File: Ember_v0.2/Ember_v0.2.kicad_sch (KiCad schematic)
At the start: 57 parts, among them J3 DROGUE, J4 BATT_CONN, J5 MAIN, J6 MAN2, J7 DROGUE2, J8 ARM, Q1 SISA96DN-T1, Q2 SISA96DN-T1, Q3 SISA96DN-T1, Q4 SISA96DN-T1, Q5 CJ3400, U1 LDO Regulator 5v, U2 BNO055, U4 BMP280, U5 BMI160, U7 RPi Pico 2

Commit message: Roughly added the strain gauge thingy
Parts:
- added C3, C4, C8, C9: 100nF, microbuilder:0603, symbol microbuilder:CAP_CERAMIC0603
- added R10, R11, R12, R16, R18, R25, R26, R34, R35, R36, R37, R9: 330E, microbuilder:0603, symbol microbuilder:RESISTOR0603
- added U6, U8: ADS1220xPW, Package_SO:TSSOP-16_4.4x5mm_P0.65mm, symbol Analog_ADC:ADS1220xPW
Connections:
- net 3v3: now also C3.1 (P$1), C4.1 (P$1), C8.1 (P$1), C9.1 (P$1), R11.2, R18.2, R34.2, R37.2, U6.12 (AVDD), U6.13 (DVDD), U6.9 (REFP0), U8.12 (AVDD), U8.13 (DVDD), U8.9 (REFP0)
- net GND: now also C3.2 (P$2), C4.2 (P$2), C8.2 (P$2), C9.2 (P$2), R10.1, R12.1, R16.1, R25.1, R26.1, R35.1, R36.1, R9.1, U6.3 (CLK), U6.4 (DGND), U6.5 (AVSS), U6.8 (REFN0), U8.3 (CLK), U8.4 (DGND), U8.5 (AVSS), U8.8 (REFN0)
- net GPS_RX: no longer U7.P$6 (GP4)
- net GPS_TX: no longer U7.P$7 (GP5)
- net LORA_BUSY: no longer names the net of U7.P$12 (GP9)
- net LORA_CS: no longer names the net of U7.P$17 (GP13)
- net LORA_DIO1: no longer names the net of U7.P$15 (GP11)
- net LORA_MISO: no longer names the net of U7.P$11 (GP8)
- net LORA_MOSI: no longer names the net of U7.P$20 (GP15)
- net LORA_RESET: no longer names the net of U7.P$16 (GP12)
- net LORA_SCLK: no longer names the net of U7.P$19 (GP14)
- new net ACT1: R10.2, U6.11 (AIN0/REFP1)
- new net ACT2: R16.2, U6.7 (AIN2)
- new net ACT3: R26.2, U8.11 (AIN0/REFP1)
- new net ACT4: R36.2, U8.7 (AIN2)
- new net ADS_CS_1: U6.2 (~{CS})
- new net ADS_CS_2: U8.2 (~{CS})
- new net ADS_DRDY_1: U6.14 (~{DRDY})
- new net ADS_DRDY_2: U8.14 (~{DRDY})
- new net ADS_MISO: U6.15 (DOUT/~{DRDY}), U8.15 (DOUT/~{DRDY})
- new net ADS_MOSI: U6.16 (DIN), U8.16 (DIN)
- new net ADS_SCLK: U6.1 (SCLK), U8.1 (SCLK)
- new net REF1: R11.1, R9.2, U6.10 (AIN1)
- new net REF2: R12.2, R18.1, U6.6 (AIN3/REFN1)
- new net REF3: R25.2, R34.1, U8.10 (AIN1)
- new net REF4: R35.2, R37.1, U8.6 (AIN3/REFN1)
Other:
- moved on the sheet: C1, C13, C14, C15, C16, C2, C24, C25, LS2, Q1, Q2, Q3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

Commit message: anything until test launch prep
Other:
- moved on the sheet: C14, R19, R24, U4
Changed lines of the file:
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@@
 	(text "BMP280"
 		(exclude_from_sim no)
-		(at 360.934 167.386 0)
+		(at 354.584 190.246 0)
 		(effects
 			(font
@@
 	)
 	(junction
-		(at 367.03 154.94)
+		(at 360.68 177.8)
 		(diameter 0)
 		(color 0 0 0 0)
@@
 	)
 	(junction
-		(at 364.49 133.35)
+		(at 358.14 156.21)
 		(diameter 0)
 		(color 0 0 0 0)
@@
 	(wire
 		(pts
-			(xy 346.71 147.32) (xy 354.33 147.32)
+			(xy 340.36 170.18) (xy 347.98 170.18)
 		)
 		(stroke
@@
 	(wire
 		(pts
-			(xy 364.49 154.94) (xy 367.03 154.94)
+			(xy 358.14 177.8) (xy 360.68 177.8)
 		)
 		(stroke
@@
 	(wire
 		(pts
-			(xy 332.74 147.32) (xy 336.55 147.32)
+			(xy 326.39 170.18) (xy 330.2 170.18)
 		)
 		(stroke
@@
 	(wire
 		(pts
-			(xy 346.71 142.24) (xy 354.33 142.24)
+			(xy 340.36 165.1) (xy 347.98 165.1)
 		)
 		(stroke
@@
 	(wire
 		(pts
-			(xy 364.49 130.81) (xy 364.49 133.35)
+			(xy 358.14 153.67) (xy 358.14 156.21)
 		)
 		(stroke
@@
 	(wire
 		(pts
-			(xy 364.49 137.16) (xy 364.49 133.35)
+			(xy 358.14 160.02) (xy 358.14 156.21)
 		)
 		(stroke
@@
 	(wire
 		(pts
-			(xy 354.33 149.86) (xy 354.33 153.67)
+			(xy 347.98 172.72) (xy 347.98 176.53)
 		)
 		(stroke
@@
 	(wire
 		(pts
-			(xy 346.71 144.78) (xy 354.33 144.78)
+			(xy 340.36 167.64) (xy 347.98 167.64)
 		)
 		(stroke
@@
 	(wire
 		(pts
-			(xy 367.03 154.94) (xy 367.03 160.02)
+			(xy 360.68 177.8) (xy 360.68 182.88)
 		)
 		(stroke
@@
 	(wire
 		(pts
-			(xy 367.03 133.35) (xy 364.49 133.35)
+			(xy 360.68 156.21) (xy 358.14 156.21)
 		)
 		(stroke
@@
 	(wire
 		(pts
-			(xy 354.33 133.35) (xy 356.87 133.35)
+			(xy 347.98 156.21) (xy 350.52 156.21)
 		)
 		(stroke
@@
 	(wire
 		(pts
-			(xy 367.03 133.35) (xy 367.03 137.16)
+			(xy 360.68 156.21) (xy 360.68 160.02)
 		)
 		(stroke
@@
 	)
 	(label "3v3"
-		(at 344.17 153.67 0)
+		(at 337.82 176.53 0)
 		(effects
 			(font
@@
 	)
 	(label "GND"
-		(at 354.33 133.35 180)
+		(at 347.98 156.21 180)
 		(effects
 			(font
@@
 	)
 	(label "GND"
-		(at 332.74 147.32 180)
+		(at 326.39 170.18 180)
 		(effects
 			(font
@@
 	)
 	(label "GND"
-		(at 367.03 160.02 0)
+		(at 360.68 182.88 0)
 		(effects
 			(font
@@
 	)
 	(label "SCL"
-		(at 346.71 142.24 0)
+		(at 340.36 165.1 0)
 		(effects
 			(font
@@
 	)
 	(label "SDA"
-		(at 346.71 144.78 0)
+		(at 340.36 167.64 0)
 		(effects
 			(font
@@
 	)
 	(label "3v3"
-		(at 364.49 130.81 0)
+		(at 358.14 153.67 0)
 		(effects
 			(font
@@
 	(symbol
 		(lib_id "microbuilder:CAP_CERAMIC0603")
-		(at 359.41 133.35 270)
+		(at 353.06 156.21 270)
 		(unit 1)
 		(exclude_from_sim no)
@@
 		(fields_autoplaced yes)
 		(property "Reference" "C14"
-			(at 360.68 127 90)
+			(at 354.33 149.86 90)
 			(effects
 				(font
@@
 		)
 		(property "Value" "100 nF"
-			(at 360.68 129.54 90)
+			(at 354.33 152.4 90)
 			(effects
 				(font
@@
 		)
 		(property "Footprint" "microbuilder:0603"
-			(at 359.41 133.35 0)
+			(at 353.06 156.21 0)
 			(effects
 				(font
@@
 		)
 		(property "Datasheet" ""
-			(at 359.41 133.35 0)
+			(at 353.06 156.21 0)
 			(effects
 				(font
@@
 		)
 		(property "Description" "Ceramic Capacitors\n\n0402 - 0402 Surface Mount Capacitors\n\n• 16pF 50V 5% [Digikey: 445-4899-2-ND]\n• 18pF 50V 5% [Digikey: 490-1281-2-ND]\n• 22pF 50V 5% [Digikey: 490-1283-2-ND]\n• 68pF 50V 5% [Digikey: 490-1289-2-ND]\n• 0.1uF 10V 10% [Digikey: 490-1318-2-ND]\n• 1.0uF 6.3V 10% [Digikey: 490-1320-2-ND]\n\n0603 - 0603 Surface Mount Capacitors\n\n• 16 pF 50V 5% [Digikey: 445-5051-2-ND]\n• 22 pF 50V [Digikey: PCC220ACVTR-ND]\n• 33 pF 50V 5% [Digikey: 490-1415-1-ND]\n• 56pF 50V 5% [Digikey: 490-1421-1-ND]\n• 220pF 50V 5% [Digikey: 445-1285-1-ND]\n• 680 pF 50V\n• 2200 pF 50V 5% C0G [Digikey: 445-1297-1-ND]\n• 5600 pF 100V 5% X7R [Digikey: 478-3711-1-ND]\n• 0.1 µF 25V 10% [Digikey: PCC2277TR-ND]\n• 0.22 µF 16V 10% X7R [Digikey: 445-1318-1-ND]\n• 1.0 µF 25V 10% [Digikey: 445-5146-2-ND]\n\n0603 - RF Specific\n\n• 3pF 250V +/-0.1pF RF [Digikey: 712-1347-1-ND]\n• 18 pF 250V 5%  [Digikey: 478-3505-1-ND or 712-1322-1-ND]\n• 56 pF 250V 5% C0G RF [Digikey: 490-4867-1-ND]\n• 68 pF 250V RF [Digikey: 490-4868-1-ND]\n\n0805 - 0805 Surface Mount Capacitors\n\n• 220 pF 250V 2% RF Ceramic Capacitor [Digikey: 712-1398-1-ND]\n• 1000 pF 50V 2% NP0 Ceramic Capacitor [Digikey: 478-3760-1-ND]\n• 0.1 µF 25V 10% Ceramic Capacitor [Digikey: PCC1828TR-ND]\n• 1.0 µF 16V 10% Ceramic Capacitor[Digikey: 490-1691-2-ND]\n• 10.0 µF 10V 10% Ceramic Capacitor[Digikey: 709-1228-1-ND]\n• 10.0 uF 16V 10% Ceramic Capacitor [Digikey: 478-5165-2-ND]\n• 47 uF 6.3V 20% Ceramic Capacitor [Digikey: 587-1779-1-ND or 399-5506-1-ND]\n\n1206 - 1206 Surface Mount Capacitors\n\n• 47uF 10V 20% Ceramic Capacitor [Digikey: 490-5528-1-ND or 399-5508-1-ND or 445-6010-1-ND]\n• 100uF 6.3V -20%, +80% Y5V Ceramic Capacitor (Digikey: 490-4512-1-ND, Mouser: 81-GRM31CF50J107ZE1L)"
-			(at 359.41 133.35 0)
+			(at 353.06 156.21 0)
 			(effects
 				(font
@@
 	(symbol
 		(lib_id "adafruit:R-US_R0603")
-		(at 349.25 153.67 0)
+		(at 342.9 176.53 0)
 		(unit 1)
 		(exclude_from_sim no)
@@
 		(fields_autoplaced yes)
 		(property "Reference" "R24"
-			(at 349.25 146.05 0)
+			(at 342.9 168.91 0)
 			(effects
 				(font
@@
 		)
 		(property "Value" "10k ohm"
-			(at 349.25 149.86 0)
+			(at 342.9 172.72 0)
 			(effects
 				(font
@@
 		)
 		(property "Footprint" "adafruit:R0603"
-			(at 349.25 153.67 0)
+			(at 342.9 176.53 0)
 			(effects
 				(font
@@
 		)
 		(property "Datasheet" ""
-			(at 349.25 153.67 0)
+			(at 342.9 176.53 0)
 			(effects
 				(font
@@
 		)
 		(property "Description" "RESISTOR, American symbol"
-			(at 349.25 153.67 0)
+			(at 342.9 176.53 0)
 			(effects
 				(font
@@
 	(symbol
 		(lib_id "Sensor_Pressure:BMP280")
-		(at 364.49 147.32 0)
+		(at 358.14 170.18 0)
 		(unit 1)
 		(exclude_from_sim no)
@@
 		(fields_autoplaced yes)
 		(property "Reference" "U4"
-			(at 370.84 144.7799 0)
+			(at 364.49 167.6399 0)
 			(effects
 				(font
@@
 		)
 		(property "Value" "BMP280"
-			(at 370.84 147.3199 0)
+			(at 364.49 170.1799 0)
 			(effects
 				(font
@@
 		)
 		(property "Footprint" "Package_LGA:Bosch_LGA-8_2x2.5mm_P0.65mm_ClockwisePinNumbering"
-			(at 364.49 165.1 0)
+			(at 358.14 187.96 0)
 			(effects
 				(font
@@
 		)
 		(property "Datasheet" "https://ae-bst.resource.bosch.com/media/_tech/media/datasheets/BST-BMP280-DS001.pdf"
-			(at 364.49 147.32 0)
+			(at 358.14 170.18 0)
 			(effects
 				(font
@@
 		)
 		(property "Description" "Absolute Barometric Pressure Sensor, LGA-8"
-			(at 364.49 147.32 0)
+			(at 358.14 170.18 0)
 			(effects
 				(font
@@
 	(symbol
 		(lib_id "adafruit:R-US_R0603")
-		(at 341.63 147.32 0)
+		(at 335.28 170.18 0)
 		(unit 1)
 		(exclude_from_sim no)
@@
 		(fields_autoplaced yes)
 		(property "Reference" "R19"
-			(at 341.63 139.7 0)
+			(at 335.28 162.56 0)
 			(effects
 				(font
@@
 		)
 		(property "Value" "10k ohm"
-			(at 341.63 143.51 0)
+			(at 335.28 166.37 0)
 			(effects
 				(font
@@
 		)
 		(property "Footprint" "adafruit:R0603"
-			(at 341.63 147.32 0)
+			(at 335.28 170.18 0)
 			(effects
 				(font
@@
 		)
 		(property "Datasheet" ""
-			(at 341.63 147.32 0)
+			(at 335.28 170.18 0)
 			(effects
 				(font
@@
 		)
 		(property "Description" "RESISTOR, American symbol"
-			(at 341.63 147.32 0)
+			(at 335.28 170.18 0)
 			(effects
 				(font

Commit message: all until 19 mar
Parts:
- removed C2: ~, microbuilder:0603, symbol microbuilder:CAP_CERAMIC0603
- removed U5: BMI160, Package_LGA:Bosch_LGA-14_3x2.5mm_P0.5mm, symbol Sensor_Motion:BMI160
- added IC1: ~, MPXV5100DP:MPXV5100DP, symbol MPXV5100DP:MPXV5100DP
- added JP1: B2B_Conn, microbuilder:1X04_OVAL, symbol microbuilder:HEADER-1X4
- added JP2, JP3, JP4, JP5: ~, microbuilder:1X02_OVAL, symbol microbuilder:HEADER-1X2
- added LED2, LED3: ~, microbuilder:CHIPLED_0603, symbol microbuilder:LED0603
- added R38, R40, R42: 10k, microbuilder:0603, symbol microbuilder:RESISTOR0603
- added R39, R41: 13k, microbuilder:0603, symbol microbuilder:RESISTOR0603
- added R43, R44: 100, microbuilder:0603, symbol microbuilder:RESISTOR0603
- added U5: ~, ADS1115IDGSR:SOP50P490X110-10N, symbol ADS1115IDGSR:ADS1115IDGSR
- C1: value ~ -> 100nF
- R13: value 10k -> 2k
- R14: value 13k -> 3k
- R6, R8: value ~ -> 13k
- R7: value ~ -> 10k
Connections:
- net GPS_RX is gone; now on net B2B_RX: R1.2
- net GPS_TX is gone; now on net B2B_TX: R2.2
- net 3v3: now also JP2.2, JP3.2, JP4.2, JP5.2, U5.8 (VDD); no longer C1.1 (P$1), R6.2, R7.1, R8.1
- net 5v: now also C1.1 (P$1), IC1.2 (VS), JP1.1
- net ACT1: now also JP2.1
- net ACT2: now also JP3.1
- net ACT3: now also JP4.1
- net ACT4: now also JP5.1
- net ADS_CS_1: now also U7.P$17 (GP13)
- net ADS_CS_2: now also U7.P$12 (GP9)
- net ADS_DRDY_1: now also U7.P$19 (GP14)
- net ADS_DRDY_2: now also U7.P$20 (GP15)
- net ADS_MISO: now also U7.P$16 (GP12)
- net ADS_MOSI: now also U7.P$15 (GP11)
- net ADS_SCLK: now also U7.P$14 (GP10)
- net GND: now also R14.2, R7.2, IC1.3 (GND), JP1.2, LED2.C, LED3.C, R38.2, R40.2, R42.2, U5.1 (ADDR), U5.3 (GND); no longer R13.1
- net PYRO_DROGUE: now also R6.1
- net PYRO_DROGUE2: now also R8.1
- net PYRO_MAIN: now also R41.1
- net PYRO_MAIN2: now also R39.1
- net SCL: now also U5.10 (SCL); no longer R7.2
- net SDA: now also U5.9 (SDA); no longer R6.1
- net VCC_PYRO: no longer R14.2
- net KX_INT: now reaches U3.5 (INT1)
- net KX_INT: now also U7.P$25 (GP19)
- net V_DP: now reaches R13.2, R14.1
- net V_DP: now also U5.4 (AIN0); no longer U7.P$31 (GP26)
- net at U7.P$1 (GP0): now also R43.2
- net at U7.P$2 (GP1): now also R44.2
- net BNO_INT: now reaches U7.P$24 (GP18)
- net BNO_INT: now also U2.14 (INT)
- net ADS_ALERT: now reaches U7.P$29 (GP22)
- net ADS_ALERT: now also U5.2 (ALERT/RDY)
- net at U7.P$32 (GP27): now also R39.2, R40.1
- net B2B_TX: now reaches U7.P$6 (GP4)
- net B2B_TX: now also JP1.4
- net B2B_RX: now reaches U7.P$7 (GP5)
- net B2B_RX: now also JP1.3
- net at R8.2: now also R38.1, U5.7 (AIN3)
- new net: LED3.A, R44.1
- new net: IC1.4 (VOUT), R13.1
- new net: LED2.A, R43.1
- new net: R41.2, R42.1, U7.P$31 (GP26)
- new net: R6.2, R7.1, U5.6 (AIN2)
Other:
- note removed: "BMI160"

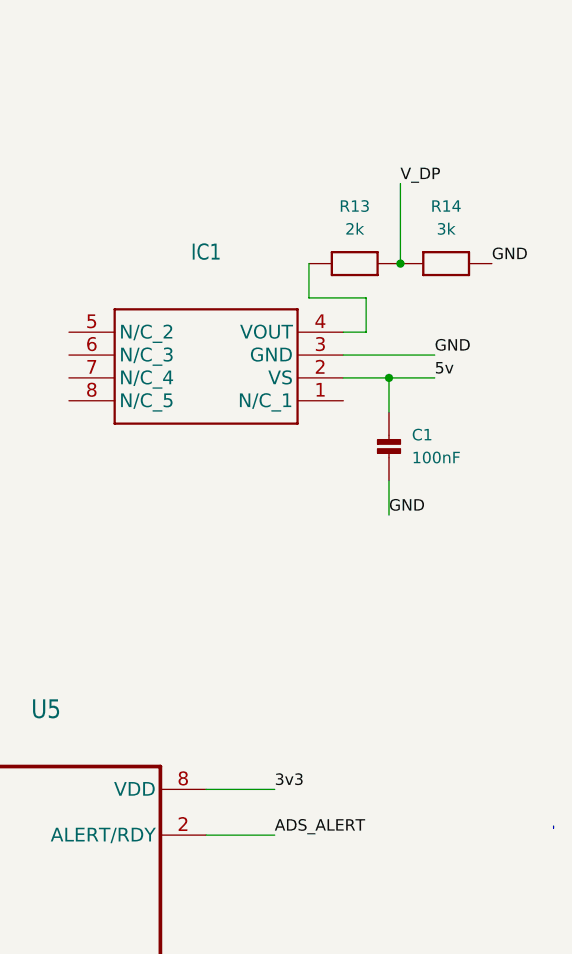
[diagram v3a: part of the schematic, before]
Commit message: Ember V0.2 routing halfway done
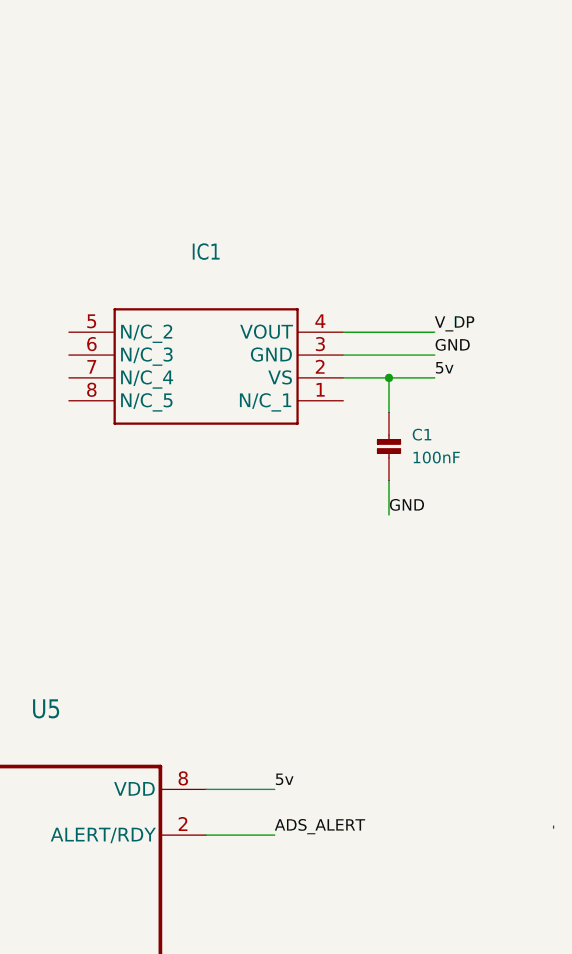
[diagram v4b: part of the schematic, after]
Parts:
- removed R13: 2k, microbuilder:0603, symbol microbuilder:RESISTOR0603
- removed R14: 3k, microbuilder:0603, symbol microbuilder:RESISTOR0603
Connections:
- net 3v3: no longer U5.8 (VDD)
- net 5v: now also U5.8 (VDD)
- net V_DP: now also IC1.4 (VOUT)
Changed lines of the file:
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@@
 	)
 	(junction
-		(at 391.16 44.45)
-		(diameter 0)
-		(color 0 0 0 0)
-	)
-	(junction
 		(at 62.23 55.88)
 		(diameter 0)
@@
 	(wire
 		(pts
-			(xy 391.16 35.56) (xy 391.16 44.45)
-		)
-		(stroke
-			(width 0)
-			(type default)
-		)
-	)
-	(wire
-		(pts
 			(xy 99.06 102.87) (xy 105.41 102.87)
 		)
@@
 	(wire
 		(pts
-			(xy 387.35 48.26) (xy 381 48.26)
-		)
-		(stroke
-			(width 0)
-			(type default)
-		)
-	)
-	(wire
-		(pts
 			(xy 74.93 31.75) (xy 78.74 31.75)
 		)
@@
 	(wire
 		(pts
-			(xy 387.35 52.07) (xy 387.35 48.26)
-		)
-		(stroke
-			(width 0)
-			(type default)
-		)
-	)
-	(wire
-		(pts
 			(xy 269.24 59.69) (xy 280.67 59.69)
 		)
@@
 	(wire
 		(pts
-			(xy 384.81 52.07) (xy 387.35 52.07)
+			(xy 384.81 52.07) (xy 394.97 52.07)
 		)
 		(stroke
@@
 	(wire
 		(pts
-			(xy 381 44.45) (xy 381 48.26)
-		)
-		(stroke
-			(width 0)
-			(type default)
-		)
-	)
-	(wire
-		(pts
 			(xy 335.28 66.04) (xy 335.28 68.58)
 		)
@@
 		)
 	)
-	(label "GND"
-		(at 401.32 44.45 0)
-		(effects
-			(font
-				(size 1.27 1.27)
-			)
-			(justify left bottom)
-		)
-	)
 	(label "V_BATT"
 		(at 153.67 236.22 180)
@@
 		)
 	)
-	(label "3v3"
+	(label "5v"
 		(at 377.19 102.87 0)
 		(effects
@@
 	)
 	(label "V_DP"
-		(at 391.16 35.56 0)
+		(at 394.97 52.07 0)
 		(effects
 			(font
@@
 	)
 	(symbol
-		(lib_id "microbuilder:RESISTOR0603")
-		(at 396.24 44.45 0)
-		(unit 1)
-		(exclude_from_sim no)
-		(in_bom yes)
-		(on_board yes)
-		(dnp no)
-		(fields_autoplaced yes)
-		(property "Reference" "R14"
-			(at 396.24 38.1 0)
-			(effects
-				(font
-					(size 1.27 1.27)
-				)
-			)
-		)
-		(property "Value" "3k"
-			(at 396.24 40.64 0)
-			(effects
-				(font
-					(size 1.27 1.27)
-				)
-			)
-		)
-		(property "Footprint" "microbuilder:0603"
-			(at 396.24 44.45 0)
-			(effects
-				(font
-					(size 1.27 1.27)
-				)
-				(hide yes)
-			)
-		)
-		(property "Datasheet" ""
-			(at 396.24 44.45 0)
-			(effects
-				(font
-					(size 1.27 1.27)
-				)
-				(hide yes)
-			)
-		)
-		(property "Description" "Resistors\n\n0402 - 0402 Surface Mount Package\n\n• 22 Ohm 1% 1/16W [Digikey: 311-22.0LRTR-ND]\n• 33 Ohm 5% 1/16W\n• 1.0K 5% 1/16W\n• 1.5K 5% 1/16W\n• 2.0K 1% 1/16W\n• 10.0K 1% 1/16W [Digikey: 311-10.0KLRTR-ND]\n• 10.0K 5% 1/16W [Digikey: RMCF0402JT10K0TR-ND]\n• 12.1K 1% 1/16W [Digikey: 311-22.0LRTR-ND]\n• 100.0K 5% 1/16W\n\n0603 - 0603 Surface Mount Package\n\n• 0 Ohm 1/10 Watt 1% Resistor\n• 15 Ohm 1/10 Watt 1% Resistor\n• 33 Ohm 1/10 Watt 1% Resistor\n• 49.9 Ohm 1/10 Watt 1% Resistor\n• 100 Ohm 1/10 Watt 1% Resistor\n• 150 Ohm 1/10 Watt 1% Resistor\n• 240 Ohm 1/10 Watt 1% Resistor\n• 390 Ohm 1/10 Watt 1% Resistor\n• 560 Ohm 1/10 Watt 1% Resistor\n• 680 Ohm 1/10 Watt 1% Resistor\n• 750 Ohm 1/10 Watt 1% Resistor\n• 1.0K Ohm 1/10 Watt 1% Resistor\n• 1.5K Ohm 1/10 Watt 1% Resistor\n• 2.0K Ohm 1/10 Watt 1% Resistor\n• 2.2K Ohm 1/10 Watt 1% Resistor\n• 3.3K Ohm 1/10 Watt 1% Resistor\n• 4.7K Ohm 1/10 Watt 1% Resistor\n• 10.0K Ohm 1/10 Watt 1% Resistor\n• 12.0K Ohm 1/10 Watt 1% Resistor\n• 12.1K Ohm 1/10 Watt 1% Resistor\n• 20.0K Ohm 1/10 Watt 1% Resistor\n• 33.0K Ohm 1/10 Watt 1% Resistor\n• 100.0K Ohm 1/10 Watt 1% Resistor\n\n0805 - 0805 Surface Mount Package\n\n• 0 Ohm 1/8 Watt 1% Resistor\n• 33 Ohm 1/8 Watt 1% Resistor\n• 100 Ohm 1/8 Watt 1% Resistor\n• 150 Ohm 1/8 Watt 1% Resistor\n• 200 Ohm 1/8 Watt 1% Resistor\n• 240 Ohm 1/8 Watt 1% Resistor\n• 330 Ohm 1/8 Watt 1% Resistor\n• 390 Ohm 1/8 Watt 1% Resistor\n• 470 Ohm 1/8 Watt 1% Resistor\n• 1.0K Ohm 1/8 Watt 1% Resistor\n• 1.5K Ohm 1/8 Watt 1% Resistor\n• 2.0K Ohm 1/8 Watt 1% Resistor\n• 4.7K Ohm 1/8 Watt 1% Resistor\n• 5.1K Ohm 1/8 Watt 1% Resistor\n• 5.6K Ohm 1/8 Watt 1% Resistor\n• 10.0K Ohm 1/8 Watt 1% Resistor\n• 22.0K Ohm 1/8 Watt 1% Resistor\n• 33.0K Ohm 1/8 Watt 1% Resistor\n• 100K Ohm 1/8 Watt 1% Resistor\n\n1206 - 1206 Surface Mount Package  2012 - 2010 Surface Mount Package\n\n• 0.11 Ohm 1/2 Watt 1% Resistor - Digikey: RHM.11UCT-ND"
-			(at 396.24 44.45 0)
-			(effects
-				(font
-					(size 1.27 1.27)
-				)
-				(hide yes)
-			)
-		)
-		(pin "1"
-		)
-		(pin "2"
-		)
-		(instances
-			(project ""
-				(path "/97e7889e-e69b-4dc1-9c2e-5339b74b36d3"
-					(reference "R14")
-					(unit 1)
-				)
-			)
-		)
-	)
-	(symbol
 		(lib_id "microbuilder:CAP_CERAMIC0603")
 		(at 115.57 81.28 0)
@@
 					(unit 1)
 				)
-			)
-		)
-	)
-	(symbol
-		(lib_id "microbuilder:RESISTOR0603")
-		(at 386.08 44.45 0)
-		(unit 1)
-		(exclude_from_sim no)
-		(in_bom yes)
-		(on_board yes)
-		(dnp no)
-		(fields_autoplaced yes)
-		(property "Reference" "R13"
-			(at 386.08 38.1 0)
-			(effects
-				(font
-					(size 1.27 1.27)
-				)
-			)
-		)
-		(property "Value" "2k"
-			(at 386.08 40.64 0)
-			(effects
-				(font
-					(size 1.27 1.27)
-				)
-			)
-		)
-		(property "Footprint" "microbuilder:0603"
-			(at 386.08 44.45 0)
-			(effects
-				(font
-					(size 1.27 1.27)
-				)
-				(hide yes)
-			)
-		)
-		(property "Datasheet" ""
-			(at 386.08 44.45 0)
-			(effects
-				(font
-					(size 1.27 1.27)
-				)
-				(hide yes)
-			)
-		)
-		(property "Description" "Resistors\n\n0402 - 0402 Surface Mount Package\n\n• 22 Ohm 1% 1/16W [Digikey: 311-22.0LRTR-ND]\n• 33 Ohm 5% 1/16W\n• 1.0K 5% 1/16W\n• 1.5K 5% 1/16W\n• 2.0K 1% 1/16W\n• 10.0K 1% 1/16W [Digikey: 311-10.0KLRTR-ND]\n• 10.0K 5% 1/16W [Digikey: RMCF0402JT10K0TR-ND]\n• 12.1K 1% 1/16W [Digikey: 311-22.0LRTR-ND]\n• 100.0K 5% 1/16W\n\n0603 - 0603 Surface Mount Package\n\n• 0 Ohm 1/10 Watt 1% Resistor\n• 15 Ohm 1/10 Watt 1% Resistor\n• 33 Ohm 1/10 Watt 1% Resistor\n• 49.9 Ohm 1/10 Watt 1% Resistor\n• 100 Ohm 1/10 Watt 1% Resistor\n• 150 Ohm 1/10 Watt 1% Resistor\n• 240 Ohm 1/10 Watt 1% Resistor\n• 390 Ohm 1/10 Watt 1% Resistor\n• 560 Ohm 1/10 Watt 1% Resistor\n• 680 Ohm 1/10 Watt 1% Resistor\n• 750 Ohm 1/10 Watt 1% Resistor\n• 1.0K Ohm 1/10 Watt 1% Resistor\n• 1.5K Ohm 1/10 Watt 1% Resistor\n• 2.0K Ohm 1/10 Watt 1% Resistor\n• 2.2K Ohm 1/10 Watt 1% Resistor\n• 3.3K Ohm 1/10 Watt 1% Resistor\n• 4.7K Ohm 1/10 Watt 1% Resistor\n• 10.0K Ohm 1/10 Watt 1% Resistor\n• 12.0K Ohm 1/10 Watt 1% Resistor\n• 12.1K Ohm 1/10 Watt 1% Resistor\n• 20.0K Ohm 1/10 Watt 1% Resistor\n• 33.0K Ohm 1/10 Watt 1% Resistor\n• 100.0K Ohm 1/10 Watt 1% Resistor\n\n0805 - 0805 Surface Mount Package\n\n• 0 Ohm 1/8 Watt 1% Resistor\n• 33 Ohm 1/8 Watt 1% Resistor\n• 100 Ohm 1/8 Watt 1% Resistor\n• 150 Ohm 1/8 Watt 1% Resistor\n• 200 Ohm 1/8 Watt 1% Resistor\n• 240 Ohm 1/8 Watt 1% Resistor\n• 330 Ohm 1/8 Watt 1% Resistor\n• 390 Ohm 1/8 Watt 1% Resistor\n• 470 Ohm 1/8 Watt 1% Resistor\n• 1.0K Ohm 1/8 Watt 1% Resistor\n• 1.5K Ohm 1/8 Watt 1% Resistor\n• 2.0K Ohm 1/8 Watt 1% Resistor\n• 4.7K Ohm 1/8 Watt 1% Resistor\n• 5.1K Ohm 1/8 Watt 1% Resistor\n• 5.6K Ohm 1/8 Watt 1% Resistor\n• 10.0K Ohm 1/8 Watt 1% Resistor\n• 22.0K Ohm 1/8 Watt 1% Resistor\n• 33.0K Ohm 1/8 Watt 1% Resistor\n• 100K Ohm 1/8 Watt 1% Resistor\n\n1206 - 1206 Surface Mount Package  2012 - 2010 Surface Mount Package\n\n• 0.11 Ohm 1/2 Watt 1% Resistor - Digikey: RHM.11UCT-ND"
-			(at 386.08 44.45 0)
-			(effects
-				(font
-					(size 1.27 1.27)
-				)
-				(hide yes)
-			)
-		)
-		(pin "1"
-		)
-		(pin "2"
-		)
-		(instances
-			(project ""
-				(path "/97e7889e-e69b-4dc1-9c2e-5339b74b36d3"
-					(reference "R13")
-					(unit 1)
-				)
